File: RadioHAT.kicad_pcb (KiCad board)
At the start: 2 copper layers, 65 x 56.5 mm, 2 parts, among them J1 RPi_GPIO

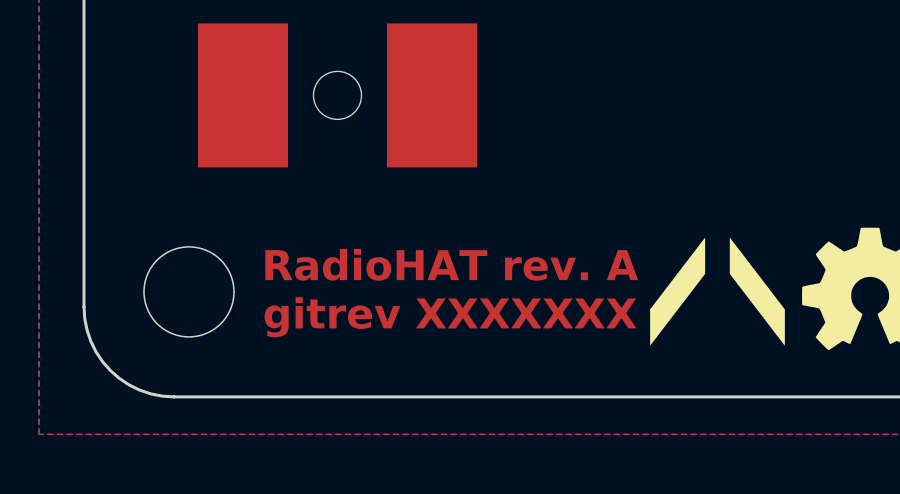
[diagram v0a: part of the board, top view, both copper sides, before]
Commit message: [PCB] Add git hash tag for CI
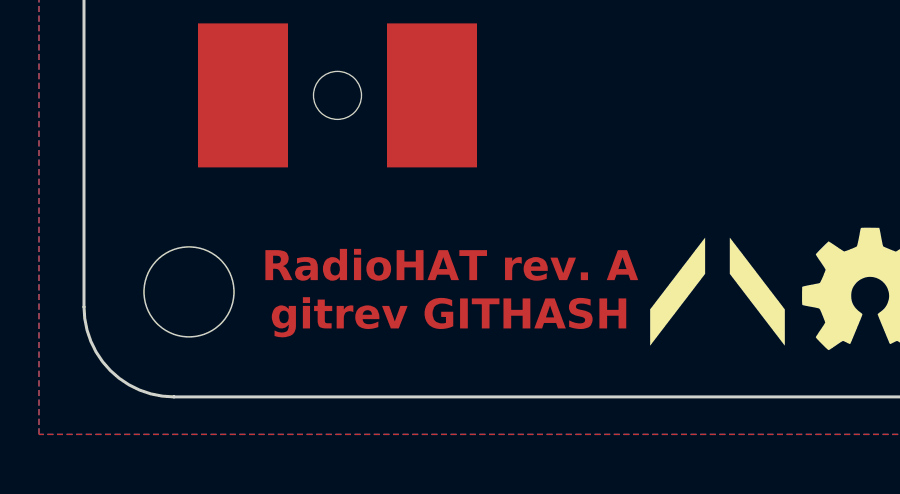
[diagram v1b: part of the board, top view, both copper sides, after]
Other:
- board text added: "RadioHAT rev. A gitrev GITHASH"
- board text removed: "RadioHAT rev. A gitrev XXXXXXX"
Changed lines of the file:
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@@
 		(layer "F.SilkS")
 	)
-	(gr_text "RadioHAT rev. A\ngitrev XXXXXXX"
+	(gr_text "RadioHAT rev. A\ngitrev GITHASH"
 		(at 119.7 123.2 0)
 		(layer "F.Cu")

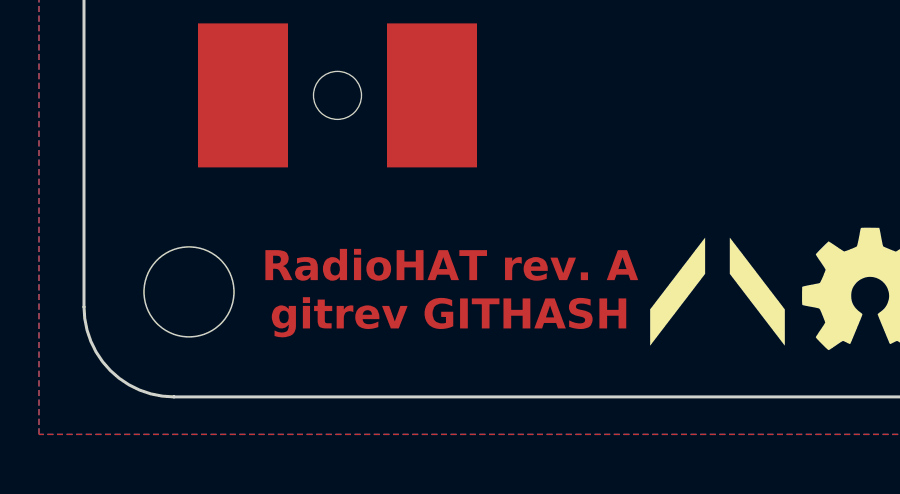
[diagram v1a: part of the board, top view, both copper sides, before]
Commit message: [PCB] Make githash variable
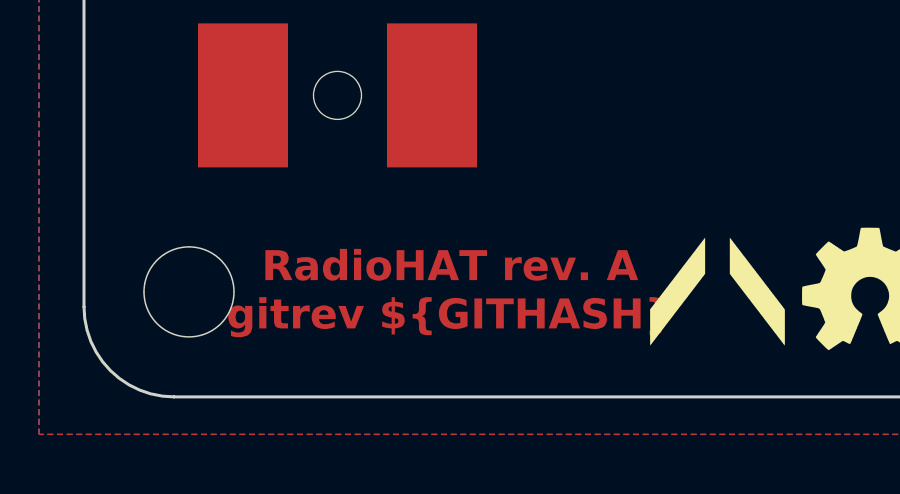
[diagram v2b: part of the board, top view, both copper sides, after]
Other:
- board text added: "RadioHAT rev. A gitrev ${GITHASH}"
- board text removed: "RadioHAT rev. A gitrev GITHASH"
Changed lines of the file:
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@@
 		(layer "F.SilkS")
 	)
-	(gr_text "RadioHAT rev. A\ngitrev GITHASH"
+	(gr_text "RadioHAT rev. A\ngitrev ${GITHASH}"
 		(at 119.7 123.2 0)
 		(layer "F.Cu")

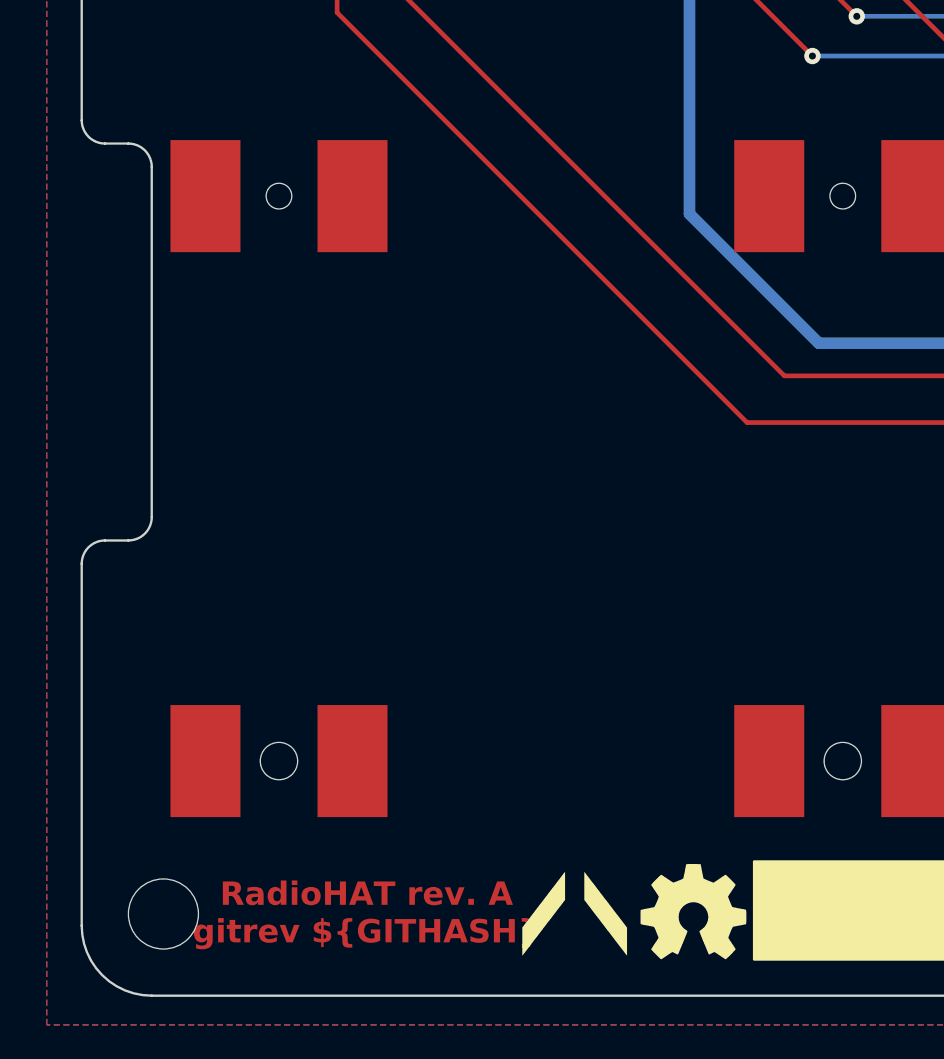
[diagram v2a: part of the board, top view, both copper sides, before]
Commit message: [PCB] Update latch footprint to make it easier to solder
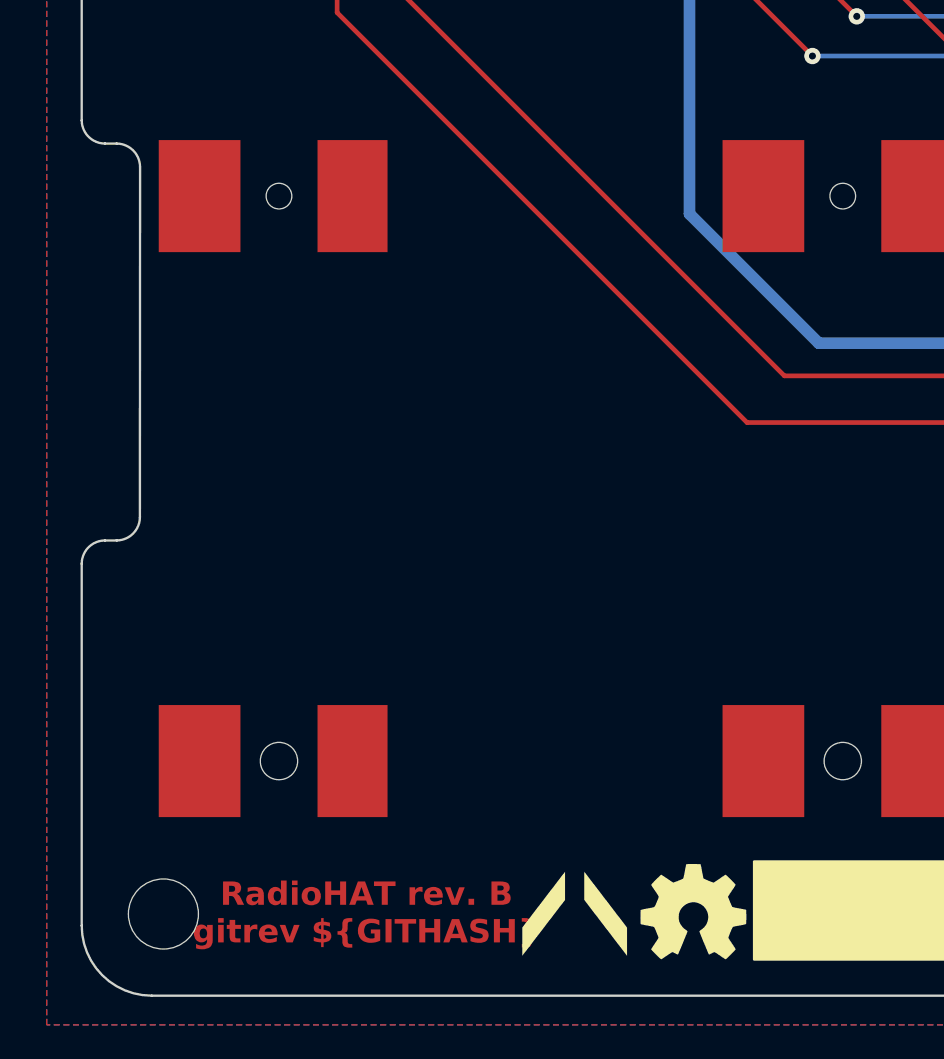
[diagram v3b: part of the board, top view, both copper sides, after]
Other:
- outline, holes or cut-outs redrawn
- board text added: "RadioHAT rev. B gitrev ${GITHASH}"
- board text removed: "RadioHAT rev. A gitrev ${GITHASH}"
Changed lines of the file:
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@@
 		(fp_line
 			(start -31.5 16)
-			(end -30.5 16)
+			(end -31 16)
 			(stroke
 				(width 0.1)
@@
 		(fp_line
 			(start -31.5 33)
-			(end -30.5 33)
+			(end -31 33)
+			(stroke
+				(width 0.1)
+				(type solid)
+			)
+			(layer "Edge.Cuts")
+		)
+		(fp_line
+			(start -30 17)
+			(end -30.007107 32)
 			(stroke
 				(width 0.1)
@@
 			(start -29.5 -4)
 			(end 29.5 -4)
-			(stroke
-				(width 0.1)
-				(type solid)
-			)
-			(layer "Edge.Cuts")
-		)
-		(fp_line
-			(start -29.5 17)
-			(end -29.5 32)
 			(stroke
 				(width 0.1)
@@
 		)
 		(fp_arc
-			(start -30.5 16)
-			(mid -29.792893 16.292893)
-			(end -29.5 17)
+			(start -31 16)
+			(mid -30.292449 16.297474)
+			(end -29.999975 17.007107)
 			(stroke
 				(width 0.1)
@@
 		)
 		(fp_arc
-			(start -29.5 32)
-			(mid -29.792893 32.707107)
-			(end -30.5 33)
+			(start -30.007082 32)
+			(mid -30.297474 32.704608)
+			(end -31 33)
 			(stroke
 				(width 0.1)
@@
 			(layer "Dwgs.User")
 			(pts
-				(xy 110.5 90.25) (xy 107.5 90.25)
+				(xy 110 90.25) (xy 107.5 90.25)
 			)
 			(height 2)
@@
 				(keep_text_aligned yes)
 			)
-			(gr_text "3,0000 mm"
-				(at 109 86.6 0)
+			(gr_text "2,5000 mm"
+				(at 108.75 86.6 0)
 				(layer "Dwgs.User")
 				(effects
@@
 			)
 		)
+		(property "Connector" "TE 1775838-2"
+			(at 0 0 90)
+			(layer "F.Fab")
+			(hide yes)
+			(effects
+				(font
+					(size 1 1)
+					(thickness 0.1)
+				)
+			)
+		)
+		(property "Latch" "Molex 48099-5701"
+			(at 0 0 90)
+			(layer "F.Fab")
+			(hide yes)
+			(effects
+				(font
+					(size 1 1)
+					(thickness 0.1)
+				)
+			)
+		)
 		(property "Mouser" "571-1775838-2"
 			(at 0 0 90)
@@
 		)
 		(fp_line
-			(start 18.2 -59.3)
+			(start 18.2 -60)
 			(end 18.2 1.3)
 			(stroke
@@
 		)
 		(fp_line
-			(start -13.8 -59.3)
-			(end 18.2 -59.3)
+			(start -13.8 -60)
+			(end 18.2 -60)
 			(stroke
 				(width 0.05)
@@
 		(fp_line
 			(start -13.8 1.3)
-			(end -13.8 -59.3)
+			(end -13.8 -60)
 			(stroke
 				(width 0.05)
@@
 		)
 		(pad "55" smd rect
-			(at -9.9 -33.5 90)
-			(size 4.8 3)
+			(at -9.9 -33.75 90)
+			(size 4.8 3.5)
 			(layers "F.Cu" "F.Mask" "F.Paste")
 			(net 2 "GND")
@@
 		)
 		(pad "56" smd rect
-			(at 14.3 -33.5 90)
-			(size 4.8 3)
+			(at 14.3 -33.75 90)
+			(size 4.8 3.5)
 			(layers "F.Cu" "F.Mask" "F.Paste")
 			(net 2 "GND")
@@
 		)
 		(pad "57" smd rect
-			(at -9.9 -57.65 90)
-			(size 4.8 3)
+			(at -9.9 -57.9 90)
+			(size 4.8 3.5)
 			(layers "F.Cu" "F.Mask" "F.Paste")
 			(net 2 "GND")
@@
 		)
 		(pad "58" smd rect
-			(at 14.3 -57.65 90)
-			(size 4.8 3)
+			(at 14.3 -57.9 90)
+			(size 4.8 3.5)
 			(layers "F.Cu" "F.Mask" "F.Paste")
 			(net 2 "GND")
@@
 		(layer "F.SilkS")
 	)
-	(gr_text "RadioHAT rev. A\ngitrev ${GITHASH}"
+	(gr_text "RadioHAT rev. B\ngitrev ${GITHASH}"
 		(at 119.7 123.2 0)
 		(layer "F.Cu")

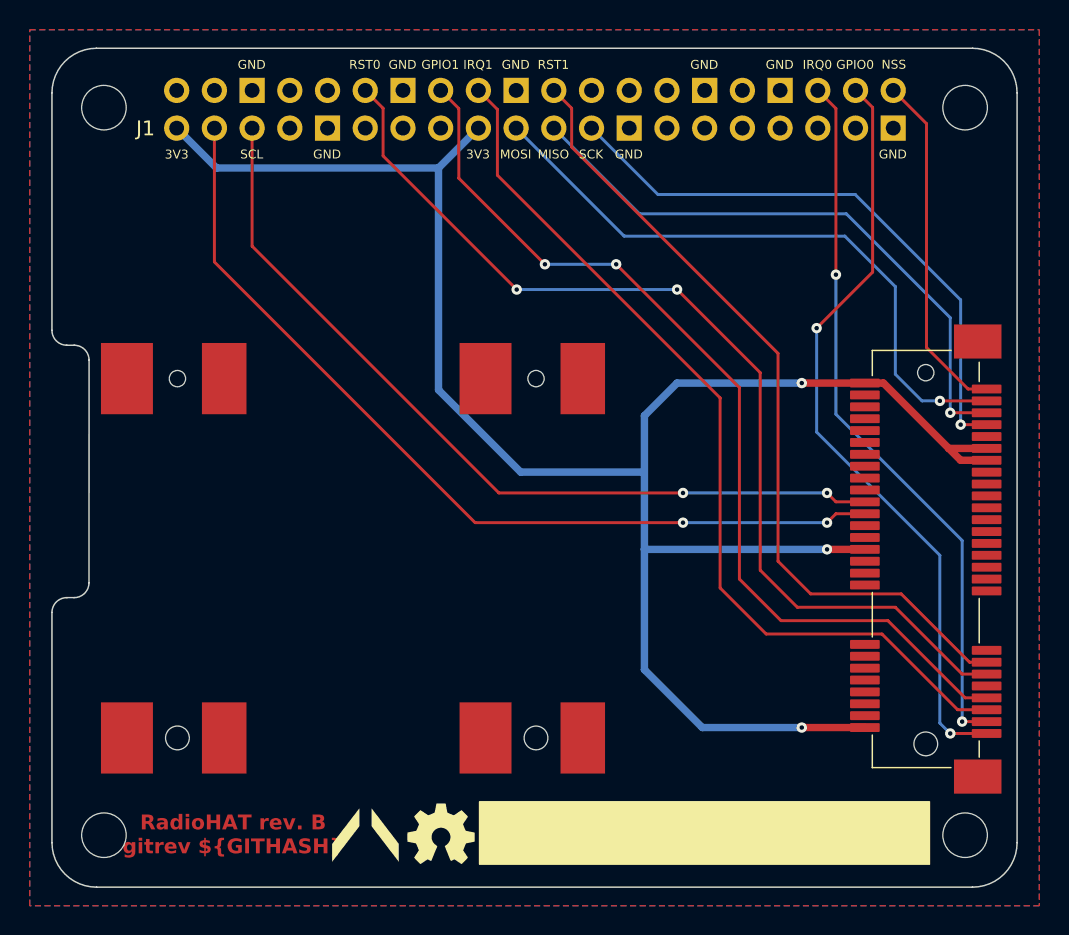
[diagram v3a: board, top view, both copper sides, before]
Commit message: HAT rev C (GPIO sense, current measure, LDO)
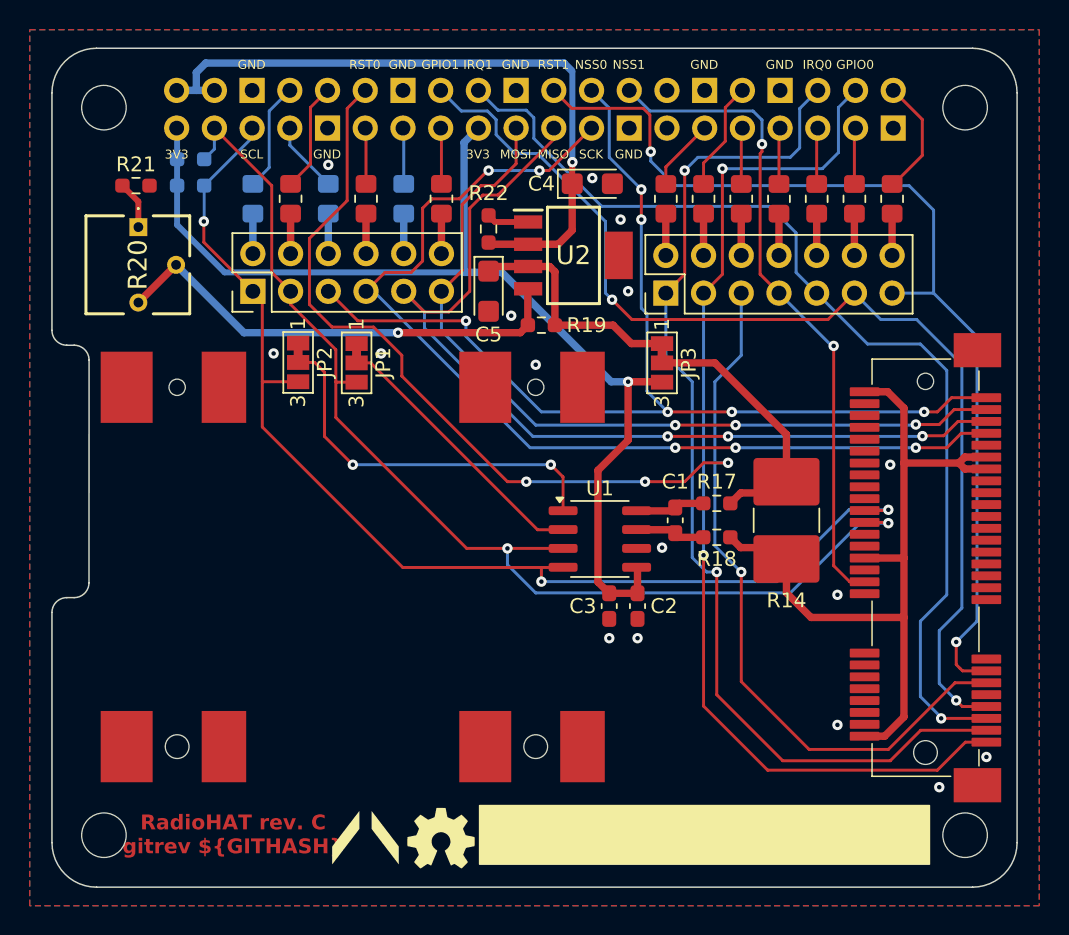
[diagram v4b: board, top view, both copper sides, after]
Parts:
- added C1: 100n, Capacitor_SMD:C_0603_1608Metric_Pad1.08x0.95mm_HandSolder, F.Cu at (149.5, 102.0)
- added C2: 100n, Capacitor_SMD:C_0603_1608Metric_Pad1.08x0.95mm_HandSolder, F.Cu at (146.9, 107.8)
- added C3: 10u, Capacitor_SMD:C_0603_1608Metric_Pad1.08x0.95mm_HandSolder, F.Cu at (145.0, 107.8)
- added C4: 10u, Capacitor_Tantalum_SMD:CP_EIA-3216-18_Kemet-A, F.Cu at (143.9, 79.4)
- added C5: 10u, Capacitor_Tantalum_SMD:CP_EIA-3216-18_Kemet-A, F.Cu at (136.9, 86.6)
- added J3: Conn_02x06_Odd_Even, Connector_PinHeader_2.54mm:PinHeader_2x06_P2.54mm_Vertical, F.Cu at (121.0, 86.6)
- added J4: Conn_02x07_Odd_Even, Connector_PinHeader_2.54mm:PinHeader_2x07_P2.54mm_Vertical, F.Cu at (148.8, 86.7)
- added JP1: SolderJumper_3_Bridged12, Jumper:SolderJumper-3_P1.3mm_Bridged12_Pad1.0x1.5mm_NumberLabels, F.Cu at (128.0, 91.4)
- added JP2: SolderJumper_3_Bridged12, Jumper:SolderJumper-3_P1.3mm_Bridged12_Pad1.0x1.5mm_NumberLabels, F.Cu at (124.1, 91.4)
- added JP3: SolderJumper_3_Bridged12, Jumper:SolderJumper-3_P1.3mm_Bridged12_Pad1.0x1.5mm_NumberLabels, F.Cu at (148.6, 91.4)
- added R1: 1k, Resistor_SMD:R_0805_2012Metric_Pad1.20x1.40mm_HandSolder, B.Cu at (121.0, 80.4)
- added R10: 1k, Resistor_SMD:R_0805_2012Metric_Pad1.20x1.40mm_HandSolder, F.Cu at (156.5, 80.4)
- added R11: 1k, Resistor_SMD:R_0805_2012Metric_Pad1.20x1.40mm_HandSolder, F.Cu at (159.0, 80.4)
- added R12: 1k, Resistor_SMD:R_0805_2012Metric_Pad1.20x1.40mm_HandSolder, F.Cu at (161.5, 80.4)
- added R13: 1k, Resistor_SMD:R_0805_2012Metric_Pad1.20x1.40mm_HandSolder, F.Cu at (164.1, 80.4)
- added R14: 100m, Resistor_SMD:R_2816_7142Metric_Pad3.20x4.45mm_HandSolder, F.Cu at (157.0, 102.0)
- added R15: 10k, Resistor_SMD:R_0603_1608Metric_Pad0.98x0.95mm_HandSolder, B.Cu at (116.8, 77.7)
- added R16: 10k, Resistor_SMD:R_0603_1608Metric_Pad0.98x0.95mm_HandSolder, B.Cu at (116.8, 79.5)
- added R17: 10R, Resistor_SMD:R_0603_1608Metric_Pad0.98x0.95mm_HandSolder, F.Cu at (152.3, 100.9)
- added R18: 10R, Resistor_SMD:R_0603_1608Metric_Pad0.98x0.95mm_HandSolder, F.Cu at (152.3, 103.2)
- added R19: 100R, Resistor_SMD:R_0603_1608Metric_Pad0.98x0.95mm_HandSolder, F.Cu at (140.5, 88.9)
- added R2: 1k, Resistor_SMD:R_0805_2012Metric_Pad1.20x1.40mm_HandSolder, F.Cu at (123.6, 80.4)
- added R20: 18R, RadioHAT:3362P1200LF, F.Cu at (113.3, 82.3)
- added R21: 51R, Resistor_SMD:R_0603_1608Metric_Pad0.98x0.95mm_HandSolder, F.Cu at (113.2, 79.5)
- added R22: 10k, Resistor_SMD:R_0603_1608Metric_Pad0.98x0.95mm_HandSolder, F.Cu at (136.9, 82.4)
- added R3: 1k, Resistor_SMD:R_0805_2012Metric_Pad1.20x1.40mm_HandSolder, B.Cu at (126.1, 80.4)
- added R4: 1k, Resistor_SMD:R_0805_2012Metric_Pad1.20x1.40mm_HandSolder, F.Cu at (128.7, 80.4)
- added R5: 1k, Resistor_SMD:R_0805_2012Metric_Pad1.20x1.40mm_HandSolder, B.Cu at (131.2, 80.4)
- added R6: 1k, Resistor_SMD:R_0805_2012Metric_Pad1.20x1.40mm_HandSolder, F.Cu at (133.7, 80.4)
- added R7: 1k, Resistor_SMD:R_0805_2012Metric_Pad1.20x1.40mm_HandSolder, F.Cu at (148.8, 80.4)
- added R8: 1k, Resistor_SMD:R_0805_2012Metric_Pad1.20x1.40mm_HandSolder, F.Cu at (151.4, 80.4)
- added R9: 1k, Resistor_SMD:R_0805_2012Metric_Pad1.20x1.40mm_HandSolder, F.Cu at (153.9, 80.4)
- added U1: INA219AxD, Package_SO:SOIC-8_3.9x4.9mm_P1.27mm, F.Cu at (144.4, 103.3)
- added U2: LP3855-ADJ, RadioHAT:SOT150P700X180-5N, F.Cu at (142.6, 84.2)
- moved J2 0.58 mm to (170.4, 107.4)
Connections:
- J1 pad 10: unconnected-(J1-BCM15_RXD-Pad10) -> SDA_SENSE
- J1 pad 11: unconnected-(J1-BCM17-Pad11) -> SPI_SCK_SENSE
- J1 pad 13: unconnected-(J1-BCM27-Pad13) -> SPI_MISO_SENSE
- J1 pad 15: unconnected-(J1-BCM22-Pad15) -> SPI_MOSI_SENSE
- J1 pad 2: unconnected-(J1-5V-Pad2) -> +5V
- J1 pad 24: unconnected-(J1-BCM8_CE0-Pad24) -> NSS0
- J1 pad 26: unconnected-(J1-BCM7_CE1-Pad26) -> NSS1
- J1 pad 29: unconnected-(J1-BCM5-Pad29) -> IRQ0_SENSE
- J1 pad 31: unconnected-(J1-BCM6-Pad31) -> RST0_SENSE
- J1 pad 32: unconnected-(J1-BCM12_PWM0-Pad32) -> GPIO0_SENSE
- J1 pad 33: unconnected-(J1-BCM13_PWM1-Pad33) -> NSS1_SENSE
- J1 pad 35: unconnected-(J1-BCM19_MISO_PCM_FS-Pad35) -> IRQ1_SENSE
- J1 pad 37: unconnected-(J1-BCM26-Pad37) -> GPIO1_SENSE
- J1 pad 4: unconnected-(J1-5V-Pad4) -> +5V
- J1 pad 40: NSS -> RST1_SENSE
- J1 pad 7: unconnected-(J1-BCM4_GPCLK0-Pad7) -> NSS0_SENSE
- J1 pad 8: unconnected-(J1-BCM14_TXD-Pad8) -> SCL_SENSE
- J2 pad 2: +3.3V -> +3.3V_PCI
- J2 pad 20: (no net) -> NSS1
- J2 pad 24: +3.3V -> +3.3V_PCI
- J2 pad 39: +3.3V -> +3.3V_PCI
- J2 pad 41: +3.3V -> +3.3V_PCI
- J2 pad 51: NSS -> NSS0
- J2 pad 52: +3.3V -> +3.3V_PCI
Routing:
- net NSS0: track 0.00 -> 72.5 mm, vias 0 -> 6
- net +3.3V: track 130.7 -> 73.5 mm, vias 3 -> 1
- net +3.3V_PCI: track 0.00 -> 52.8 mm
- net +5V: track 0.00 -> 46.3 mm, vias 0 -> 1
- net NSS1: track 0.00 -> 44.5 mm, vias 0 -> 2
- net Net-(U2-ADJ): track 0.00 -> 31.6 mm, vias 0 -> 1
- net RST0: track 67.8 -> 99.2 mm, vias 2 -> 4
- net SCK: track 39.8 -> 68.4 mm, vias 1 -> 5
- net Net-(JP2-C): track 0.00 -> 25.9 mm, vias 0 -> 2
- net NSS: track 23.4 -> 0.00 mm
- net IRQ0: track 48.2 -> 71.4 mm
- net MISO: track 40.8 -> 63.9 mm, vias 1 -> 3
- net SCL: track 56.4 -> 77.7 mm, vias 2 -> 3
- net GPIO0: track 51.5 -> 71.3 mm
- net Net-(JP1-C): track 0.00 -> 18.6 mm
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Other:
- board text added: "RadioHAT rev. C gitrev ${GITHASH}"
- board text removed: "RadioHAT rev. B gitrev ${GITHASH}"
